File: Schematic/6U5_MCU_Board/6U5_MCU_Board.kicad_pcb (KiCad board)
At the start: 2 copper layers, 20 x 52 mm, 28 parts, among them J1 Pin header, J2 EMI Shield, J3 FFC8, J4 Display interface, Q1 BC847C, U1 MCP6001T-I/OT, U2 STM32F103CBTx, U3 NCP1117-3.3_SOT223, Y1 XC32M4-8.000 12pF

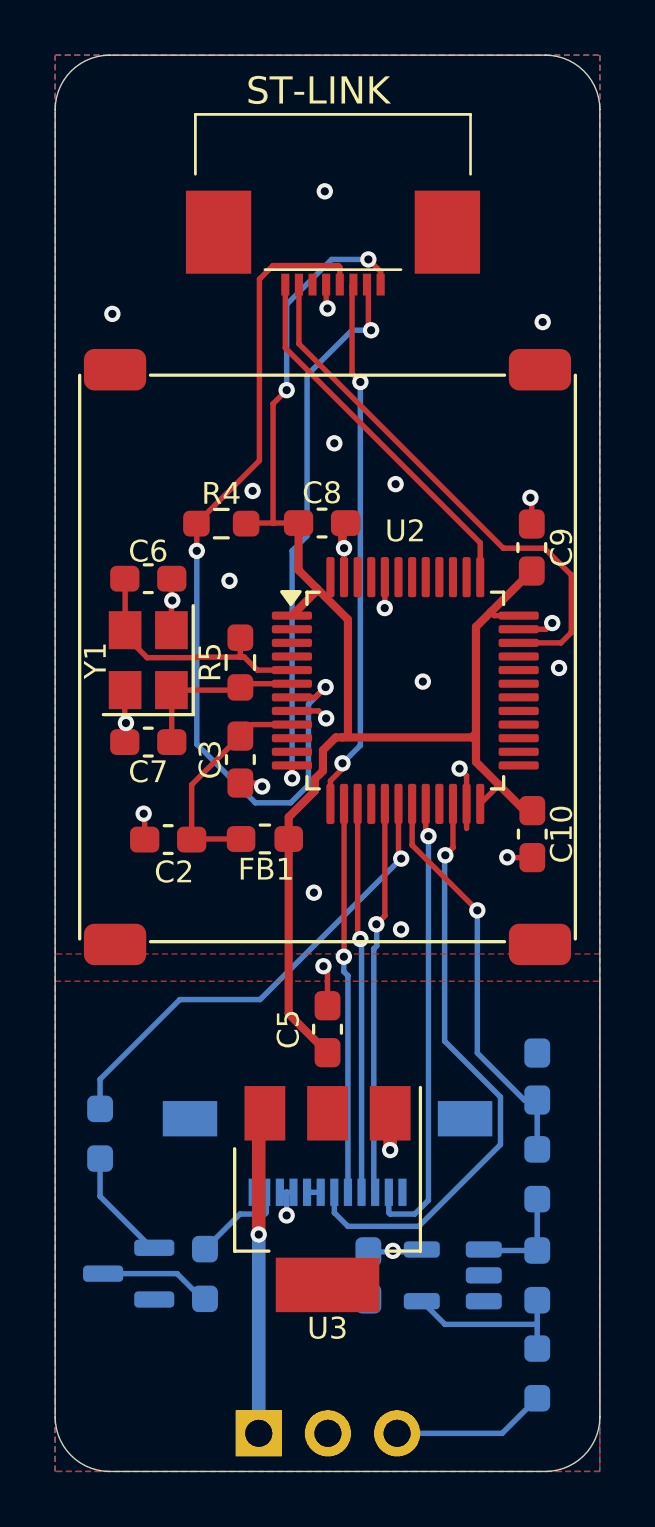
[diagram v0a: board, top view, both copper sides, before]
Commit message: Brightness and color adjustment
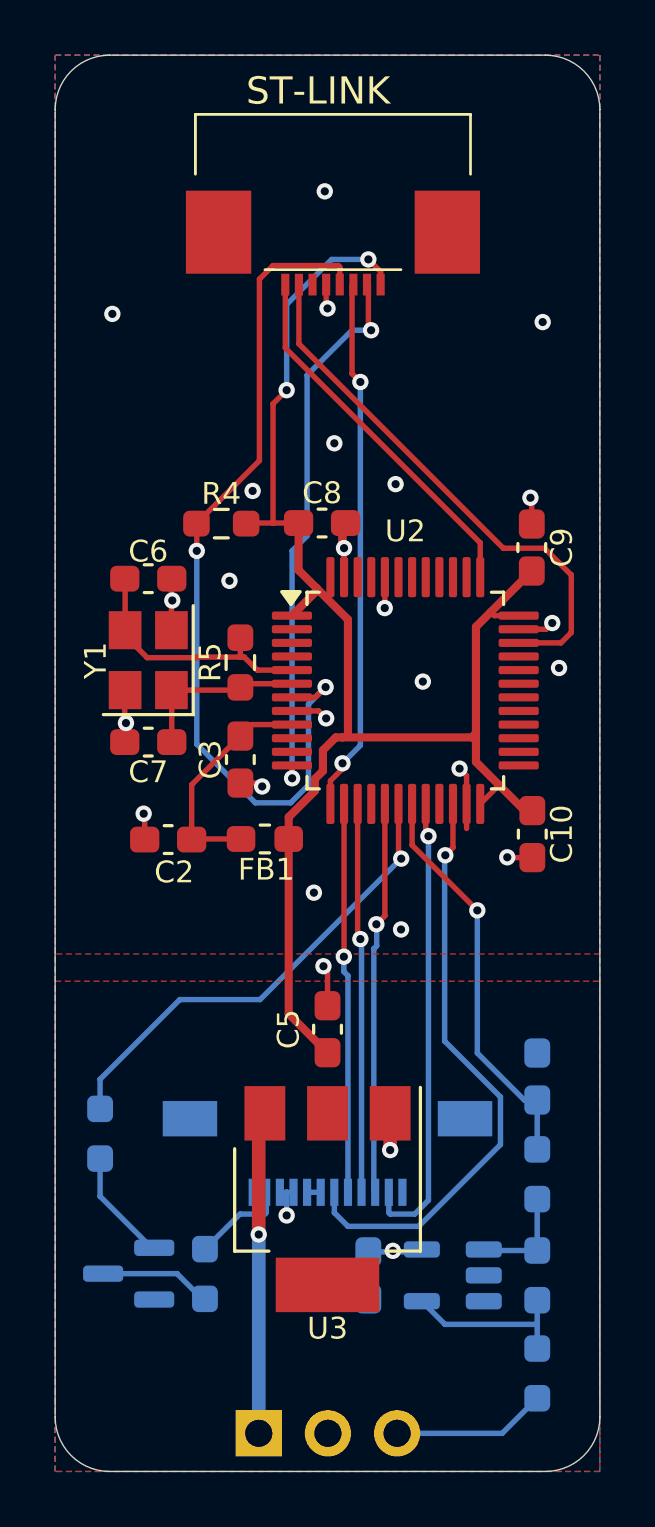
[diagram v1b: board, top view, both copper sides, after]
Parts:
- removed J2: EMI Shield, Retronics_Hardware:EMI_Shield_MS207-10S
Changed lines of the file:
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@@
-		)
-	)
-	(footprint "Retronics_Hardware:EMI_Shield_MS207-10S"
-		(layer "F.Cu")
-		(at 155.7 59.75 -90)
-		(property "Reference" "J2"
-			(at 0 -0.5 -90)
-			(unlocked yes)
-			(layer "F.SilkS")
-			(hide yes)
-			(effects
-				(font
-					(size 1 1)
-					(thickness 0.15)
-				)
-			)
-		)
-		(property "Value" "EMI Shield"
-			(at 0 1 -90)
-			(unlocked yes)
-			(layer "F.Fab")
-			(effects
-				(font
-					(size 1 1)
-					(thickness 0.15)
-				)
-			)
-		)
-		(property "Footprint" "Retronics_Hardware:EMI_Shield_MS207-10S"
-			(at 0 0 90)
-			(layer "F.Fab")
-			(hide yes)
-			(effects
-				(font
-					(size 1.27 1.27)
-					(thickness 0.15)
-				)
-			)
-		)
-		(property "Datasheet" ""
-			(at 0 0 90)
-			(layer "F.Fab")
-			(hide yes)
-			(effects
-				(font
-					(size 1.27 1.27)
-					(thickness 0.15)
-				)
-			)
-		)
-		(property "Description" ""
-			(at 0 0 90)
-			(layer "F.Fab")
-			(hide yes)
-			(effects
-				(font
-					(size 1.27 1.27)
-					(thickness 0.15)
-				)
-			)
-		)
-		(property "Comments" ""
-			(at 0 0 -90)
-			(unlocked yes)
-			(layer "F.Fab")
-			(hide yes)
-			(effects
-				(font
-					(size 1 1)
-					(thickness 0.15)
-				)
-			)
-		)
-		(property ki_fp_filters "Connector*:*_1x??_*")
-		(sheetname "Root")
-		(sheetfile "U6A_MCU_Board.kicad_sch")
-		(attr smd)
-		(fp_line
-			(start 20.7 14.8)
-			(end 0 14.8)
-			(stroke
-				(width 0.12)
-				(type default)
-			)
-			(layer "F.SilkS")
-		)
-		(fp_line
-			(start 0 12.2)
-			(end 0 -0.8)
-			(stroke
-				(width 0.12)
-				(type default)
-			)
-			(layer "F.SilkS")
-		)
-		(fp_line
-			(start 20.8 -0.8)
-			(end 20.8 12.2)
-			(stroke
-				(width 0.12)
-				(type default)
-			)
-			(layer "F.SilkS")
-		)
-		(fp_line
-			(start 0 -3.4)
-			(end 20.7 -3.4)
-			(stroke
-				(width 0.12)
-				(type default)
-			)
-			(layer "F.SilkS")
-		)
-		(fp_text user "${REFERENCE}"
-			(at 0 2.5 -90)
-			(unlocked yes)
-			(layer "F.Fab")
-			(effects
-				(font
-					(size 1 1)
-					(thickness 0.15)
-				)
-			)
-		)
-		(pad "1" smd roundrect
-			(at -0.2 -2.1)
-			(size 2.286 1.524)
-			(layers "F.Cu" "F.Paste" "F.Mask")
-			(roundrect_rratio 0.25)
-			(net 1 "GND")
-			(pinfunction "Pin_1")
-			(pintype "passive")
-			(thermal_bridge_angle 45)
-		)
-		(pad "1" smd roundrect
-			(at -0.2 13.5)
-			(size 2.286 1.524)
-			(layers "F.Cu" "F.Paste" "F.Mask")
-			(roundrect_rratio 0.25)
-			(net 1 "GND")
-			(pinfunction "Pin_1")
-			(pintype "passive")
-			(thermal_bridge_angle 45)
-		)
-		(pad "1" smd roundrect
-			(at 20.9 -2.1)
-			(size 2.286 1.524)
-			(layers "F.Cu" "F.Paste" "F.Mask")
-			(roundrect_rratio 0.25)
-			(net 1 "GND")
-			(pinfunction "Pin_1")
-			(pintype "passive")
-			(thermal_bridge_angle 45)
-		)
-		(pad "1" smd roundrect
-			(at 20.9 13.5)
-			(size 2.286 1.524)
-			(layers "F.Cu" "F.Paste" "F.Mask")
-			(roundrect_rratio 0.25)
-			(net 1 "GND")
-			(pinfunction "Pin_1")
-			(pintype "passive")
-			(thermal_bridge_angle 45)
-		)
-		(model ":KICAD6_3RD_PARTY:Retronics_Hardware.3dshapes/MS207-10S.stp"
-			(offset
-				(xyz 10.4 -5.7 5.5)
-			)
-			(scale
-				(xyz 1 1 1)
-			)
-			(rotate
-				(xyz -90 0 90)
-			)
 		)
 	)

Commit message: Re-attached EMI shield
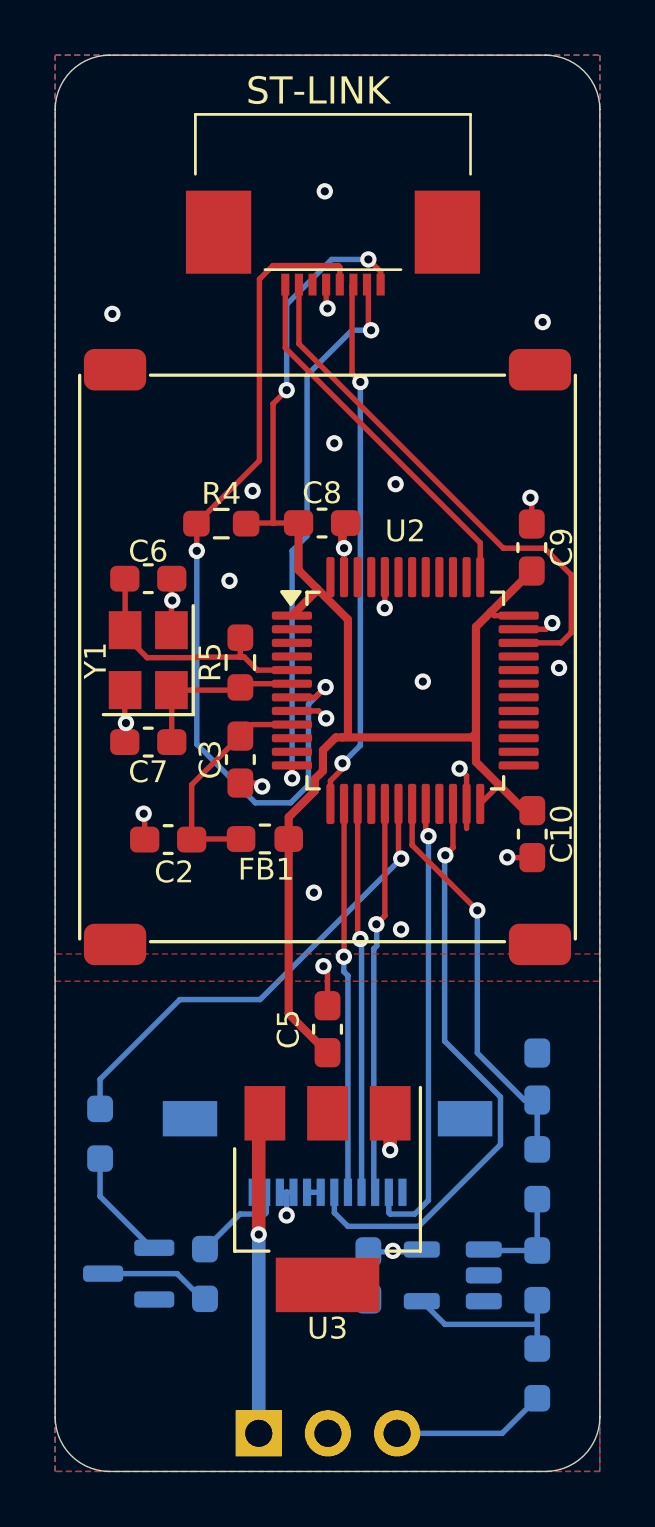
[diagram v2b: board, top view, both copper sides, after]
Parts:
- added J2: EMI Shield, Retronics_Hardware:EMI_Shield_MS207-10S, F.Cu at (155.7, 59.8)
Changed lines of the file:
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@@
 		(property ki_fp_filters "C_*")
 		(sheetname "Root")
-		(sheetfile "U6A_MCU_Board.kicad_sch")
+		(sheetfile "6U5_MCU_Board.kicad_sch")
 		(attr smd)
 		(fp_line
@@
 		(property ki_fp_filters "C_*")
 		(sheetname "Root")
-		(sheetfile "U6A_MCU_Board.kicad_sch")
+		(sheetfile "6U5_MCU_Board.kicad_sch")
 		(attr smd)
 		(fp_line
@@
 		)
 	)
+	(footprint "Retronics_Hardware:EMI_Shield_MS207-10S"
+		(layer "F.Cu")
+		(at 155.7 59.75 -90)
+		(property "Reference" "J2"
+			(at -0.000001 -0.5 -90)
+			(unlocked yes)
+			(layer "F.SilkS")
+			(hide yes)
+			(effects
+				(font
+					(size 1 1)
+					(thickness 0.15)
+				)
+			)
+		)
+		(property "Value" "EMI Shield"
+			(at 0 1.000001 -90)
+			(unlocked yes)
+			(layer "F.Fab")
+			(effects
+				(font
+					(size 1 1)
+					(thickness 0.15)
+				)
+			)
+		)
+		(property "Footprint" "Retronics_Hardware:EMI_Shield_MS207-10S"
+			(at 0 0 90)
+			(layer "F.Fab")
+			(hide yes)
+			(effects
+				(font
+					(size 1.27 1.27)
+					(thickness 0.15)
+				)
+			)
+		)
+		(property "Datasheet" ""
+			(at 0 0 90)
+			(layer "F.Fab")
+			(hide yes)
+			(effects
+				(font
+					(size 1.27 1.27)
+					(thickness 0.15)
+				)
+			)
+		)
+		(property "Description" ""
+			(at 0 0 90)
+			(layer "F.Fab")
+			(hide yes)
+			(effects
+				(font
+					(size 1.27 1.27)
+					(thickness 0.15)
+				)
+			)
+		)
+		(property "Comments" ""
+			(at 0 0 -90)
+			(unlocked yes)
+			(layer "F.Fab")
+			(hide yes)
+			(effects
+				(font
+					(size 1 1)
+					(thickness 0.15)
+				)
+			)
+		)
+		(property ki_fp_filters "Connector*:*_1x??_*")
+		(sheetname "Root")
+		(sheetfile "6U5_MCU_Board.kicad_sch")
+		(attr smd)
+		(fp_line
+			(start 20.7 14.8)
+			(end 0.000001 14.800001)
+			(stroke
+				(width 0.12)
+				(type default)
+			)
+			(layer "F.SilkS")
+		)
+		(fp_line
+			(start 0.000001 12.199999)
+			(end 0 -0.8)
+			(stroke
+				(width 0.12)
+				(type default)
+			)
+			(layer "F.SilkS")
+		)
+		(fp_line
+			(start 20.800001 -0.8)
+			(end 20.8 12.2)
+			(stroke
+				(width 0.12)
+				(type default)
+			)
+			(layer "F.SilkS")
+		)
+		(fp_line
+			(start 0 -3.4)
+			(end 20.7 -3.4)
+			(stroke
+				(width 0.12)
+				(type default)
+			)
+			(layer "F.SilkS")
+		)
+		(fp_text user "${REFERENCE}"
+			(at 0 2.5 -90)
+			(unlocked yes)
+			(layer "F.Fab")
+			(effects
+				(font
+					(size 1 1)
+					(thickness 0.15)
+				)
+			)
+		)
+		(pad "1" smd roundrect
+			(at -0.2 13.5)
+			(size 2.286 1.524)
+			(layers "F.Cu" "F.Paste" "F.Mask")
+			(roundrect_rratio 0.25)
+			(net 1 "GND")
+			(pinfunction "Pin_1")
+			(pintype "passive")
+			(thermal_bridge_angle 45)
+		)
+		(pad "1" smd roundrect
+			(at -0.199999 -2.1)
+			(size 2.286 1.524)
+			(layers "F.Cu" "F.Paste" "F.Mask")
+			(roundrect_rratio 0.25)
+			(net 1 "GND")
+			(pinfunction "Pin_1")
+			(pintype "passive")
+			(thermal_bridge_angle 45)
+		)
+		(pad "1" smd roundrect
+			(at 20.899999 -2.1)
+			(size 2.286 1.524)
+			(layers "F.Cu" "F.Paste" "F.Mask")
+			(roundrect_rratio 0.25)
+			(net 1 "GND")
+			(pinfunction "Pin_1")
+			(pintype "passive")
+			(thermal_bridge_angle 45)
+		)
+		(pad "1" smd roundrect
+			(at 20.9 13.5)
+			(size 2.286 1.524)
+			(layers "F.Cu" "F.Paste" "F.Mask")
+			(roundrect_rratio 0.25)
+			(net 1 "GND")
+			(pinfunction "Pin_1")
+			(pintype "passive")
+			(thermal_bridge_angle 45)
+		)
+		(model ":KICAD6_3RD_PARTY:Retronics_Hardware.3dshapes/MS207-10S.stp"
+			(offset
+				(xyz 10.4 -5.7 5.5)
+			)
+			(scale
+				(xyz 1 1 1)
+			)
+			(rotate
+				(xyz -90 0 90)
+			)
+		)
+	)
 	(footprint "Inductor_SMD:L_0603_1608Metric_Pad1.05x0.95mm_HandSolder"
 		(layer "F.Cu")
@@
 		(property ki_fp_filters "Inductor_* L_* *Ferrite*")
 		(sheetname "Root")
-		(sheetfile "U6A_MCU_Board.kicad_sch")
+		(sheetfile "6U5_MCU_Board.kicad_sch")
 		(attr smd)
 		(fp_line
@@
 		(property ki_fp_filters "SOT?223*TabPin2*")
 		(sheetname "Root")
-		(sheetfile "U6A_MCU_Board.kicad_sch")
+		(sheetfile "6U5_MCU_Board.kicad_sch")
 		(attr smd)
 		(fp_line
@@
 		(property ki_fp_filters "C_*")
 		(sheetname "Root")
-		(sheetfile "U6A_MCU_Board.kicad_sch")
+		(sheetfile "6U5_MCU_Board.kicad_sch")
 		(attr smd)
 		(fp_line
@@
 		(property ki_fp_filters "C_*")
 		(sheetname "Root")
-		(sheetfile "U6A_MCU_Board.kicad_sch")
+		(sheetfile "6U5_MCU_Board.kicad_sch")
 		(attr smd)
 		(fp_line
@@
 		(property ki_fp_filters "Crystal*")
 		(sheetname "Root")
-		(sheetfile "U6A_MCU_Board.kicad_sch")
+		(sheetfile "6U5_MCU_Board.kicad_sch")
 		(attr smd)
 		(fp_line
@@
 		(property ki_fp_filters "Connector*:*_1x??_*")
 		(sheetname "Root")
-		(sheetfile "U6A_MCU_Board.kicad_sch")
+		(sheetfile "6U5_MCU_Board.kicad_sch")
 		(attr smd)
 		(fp_line
@@
 		(property ki_fp_filters "R_*")
 		(sheetname "Root")
-		(sheetfile "U6A_MCU_Board.kicad_sch")
+		(sheetfile "6U5_MCU_Board.kicad_sch")
 		(attr smd)
 		(fp_line
@@
 		(property ki_fp_filters "LQFP*7x7mm*P0.5mm*")
 		(sheetname "Root")
-		(sheetfile "U6A_MCU_Board.kicad_sch")
+		(sheetfile "6U5_MCU_Board.kicad_sch")
 		(attr smd)
 		(fp_line
@@
 			(net 48 "unconnected-(U2-PA0_ADC0_PWM-Pad10)")
 			(pinfunction "PA0_ADC0_PWM")
-			(pintype "bidirectional")
+			(pintype "bidirectional+no_connect")
 		)
 		(pad "11" smd roundrect
@@
 			(net 49 "unconnected-(U2-PA1_ADC1_PWM-Pad11)")
 			(pinfunction "PA1_ADC1_PWM")
-			(pintype "bidirectional")
+			(pintype "bidirectional+no_connect")
 		)
 		(pad "12" smd roundrect
@@
 		(property ki_fp_filters "R_*")
 		(sheetname "Root")
-		(sheetfile "U6A_MCU_Board.kicad_sch")
+		(sheetfile "6U5_MCU_Board.kicad_sch")
 		(attr smd)
 		(fp_line
@@
 		(property ki_fp_filters "C_*")
 		(sheetname "Root")
-		(sheetfile "U6A_MCU_Board.kicad_sch")
+		(sheetfile "6U5_MCU_Board.kicad_sch")
 		(attr smd)
 		(fp_line
@@
 		(property ki_fp_filters "C_*")
 		(sheetname "Root")
-		(sheetfile "U6A_MCU_Board.kicad_sch")
+		(sheetfile "6U5_MCU_Board.kicad_sch")
 		(attr smd)
 		(fp_line
@@
 		(property ki_fp_filters "C_*")
 		(sheetname "Root")
-		(sheetfile "U6A_MCU_Board.kicad_sch")
+		(sheetfile "6U5_MCU_Board.kicad_sch")
 		(attr smd)
 		(fp_line
@@
 		(property ki_fp_filters "C_*")
 		(sheetname "Root")
-		(sheetfile "U6A_MCU_Board.kicad_sch")
+		(sheetfile "6U5_MCU_Board.kicad_sch")
 		(attr smd)
 		(fp_line
@@
 		(property ki_fp_filters "R_*")
 		(sheetname "Root")
-		(sheetfile "U6A_MCU_Board.kicad_sch")
+		(sheetfile "6U5_MCU_Board.kicad_sch")
 		(attr smd)
 		(fp_line
@@
 		(property ki_fp_filters "R_*")
 		(sheetname "Root")
-		(sheetfile "U6A_MCU_Board.kicad_sch")
+		(sheetfile "6U5_MCU_Board.kicad_sch")
 		(attr smd)
 		(fp_line
@@
 		(property ki_fp_filters "R_*")
 		(sheetname "Root")
-		(sheetfile "U6A_MCU_Board.kicad_sch")
+		(sheetfile "6U5_MCU_Board.kicad_sch")
 		(attr smd)
 		(fp_line
@@
 		(property ki_fp_filters "C_*")
 		(sheetname "Root")
-		(sheetfile "U6A_MCU_Board.kicad_sch")
+		(sheetfile "6U5_MCU_Board.kicad_sch")
 		(attr smd)
 		(fp_line
@@
 		(property ki_fp_filters "SOT?23*")
 		(sheetname "Root")
-		(sheetfile "U6A_MCU_Board.kicad_sch")
+		(sheetfile "6U5_MCU_Board.kicad_sch")
 		(attr smd)
 		(fp_line
@@
 		(property ki_fp_filters "Connector*:*_1x??_*")
 		(sheetname "Root")
-		(sheetfile "U6A_MCU_Board.kicad_sch")
+		(sheetfile "6U5_MCU_Board.kicad_sch")
 		(attr smd)
 		(fp_line
@@
 		(property ki_fp_filters "SOT?23*")
 		(sheetname "Root")
-		(sheetfile "U6A_MCU_Board.kicad_sch")
+		(sheetfile "6U5_MCU_Board.kicad_sch")
 		(attr smd)
 		(fp_line
@@
 		(property ki_fp_filters "R_*")
 		(sheetname "Root")
-		(sheetfile "U6A_MCU_Board.kicad_sch")
+		(sheetfile "6U5_MCU_Board.kicad_sch")
 		(attr smd)
 		(fp_line
@@
 		(property ki_fp_filters "Connector*:*_1x??_*")
 		(sheetname "Root")
-		(sheetfile "U6A_MCU_Board.kicad_sch")
+		(sheetfile "6U5_MCU_Board.kicad_sch")
 		(attr through_hole)
 		(fp_line
@@
 		(property ki_fp_filters "R_*")
 		(sheetname "Root")
-		(sheetfile "U6A_MCU_Board.kicad_sch")
+		(sheetfile "6U5_MCU_Board.kicad_sch")
 		(attr smd)
 		(fp_line
@@
 		(property ki_fp_filters "C_*")
 		(sheetname "Root")
-		(sheetfile "U6A_MCU_Board.kicad_sch")
+		(sheetfile "6U5_MCU_Board.kicad_sch")
 		(attr smd)
 		(fp_line

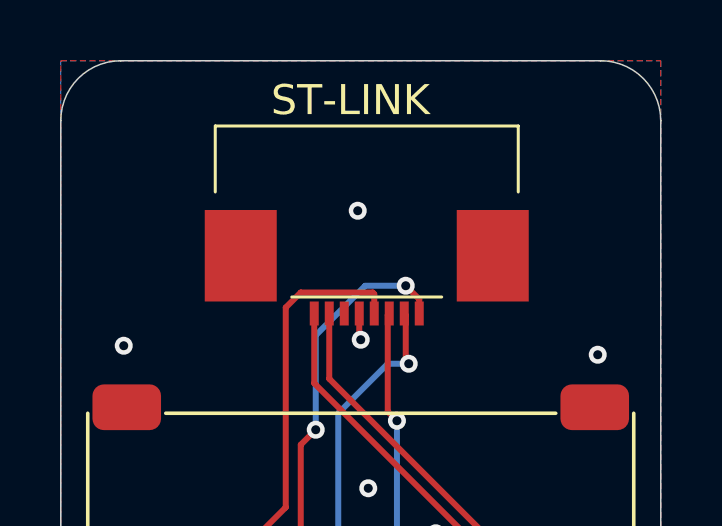
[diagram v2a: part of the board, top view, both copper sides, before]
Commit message: Added thermal reliefs on bottom ground plane
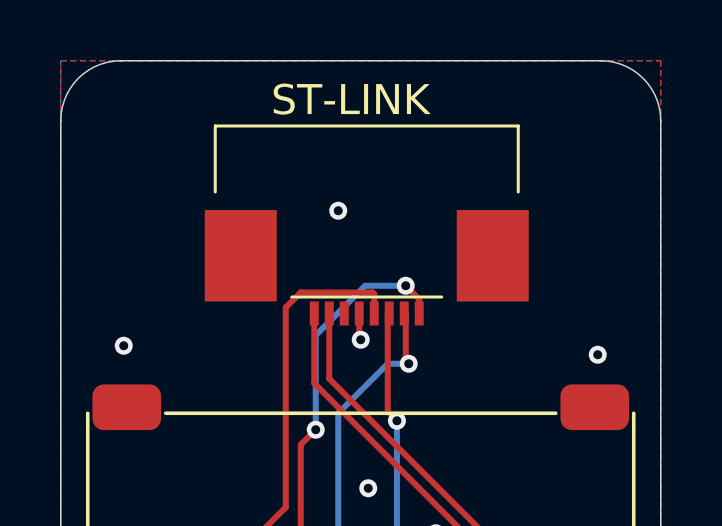
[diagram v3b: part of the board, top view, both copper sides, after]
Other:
- board text added: "6U5 MCU Board R0180B_2437 Bjørner Sandom"
- board text removed: "6U5 MCU Board R0180_2429 Bjørner Sandom"
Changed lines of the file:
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@@
 		(layer "Edge.Cuts")
 	)
-	(gr_text "6U5 MCU Board\nR0180_2429\nBjørner Sandom\n"
+	(gr_text "6U5 MCU Board\nR0180B_2437\nBjørner Sandom\n"
 		(at 150.25 55.25 0)
 		(layer "B.SilkS")
@@
 	)
 	(via
-		(at 149.9 53)
+		(at 149.25 53)
 		(size 0.6)
 		(drill 0.3)
@@
 		(hatch edge 0.5)
 		(priority 1)
-		(connect_pads yes
+		(connect_pads
 			(clearance 0.25)
 		)
